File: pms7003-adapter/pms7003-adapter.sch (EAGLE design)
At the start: 4 parts, among them J1 LPPB052CFFN-RC

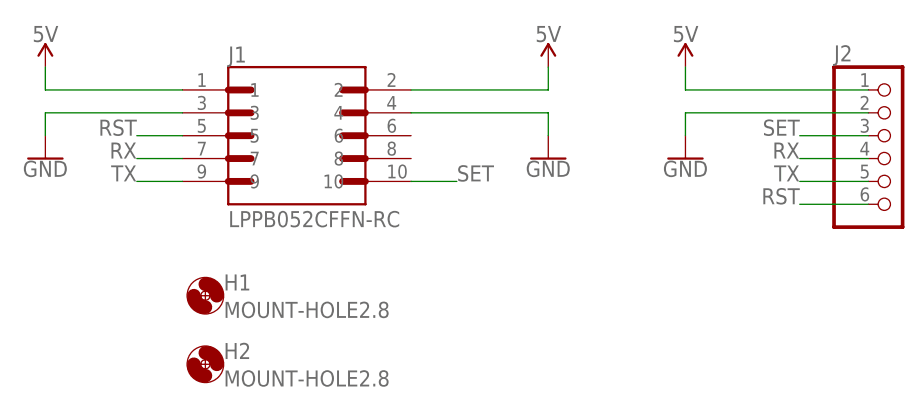
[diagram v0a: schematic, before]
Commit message: Reduced size of the PMS7003 adapter, replaced THT header with SMD header
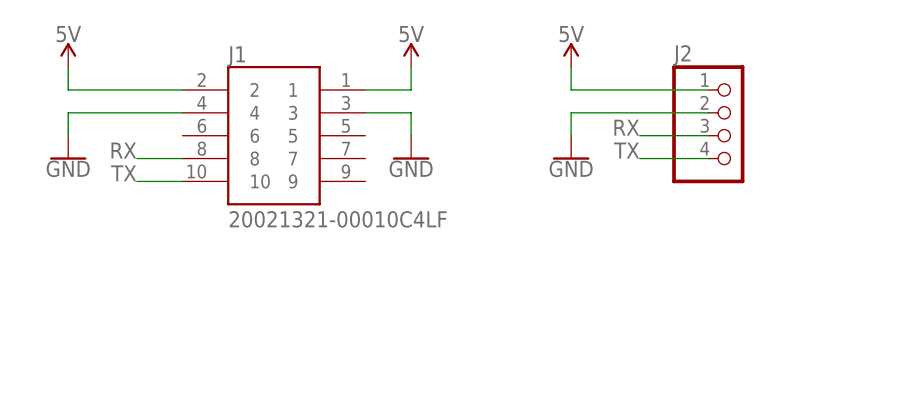
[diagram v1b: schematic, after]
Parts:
- removed H1, H2: MOUNT-HOLE2.8, holes:MOUNT-HOLE2.8
- J1: value LPPB052CFFN-RC -> 20021321-00010C4LF; device aqm-parts:LPPB052CFFN-RC -> aqm-parts:20021321-00010C4LF
- J2: device pinhead:PINHD-1X6 -> pinhead:PINHD-1X4
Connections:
- removed net RST: J1.5, J2.6
- removed net SET: J1.10, J2.3
- net RX: now also J1.8, J2.3; no longer J1.7, J2.4
- net TX: now also J1.10, J2.4; no longer J1.9, J2.5

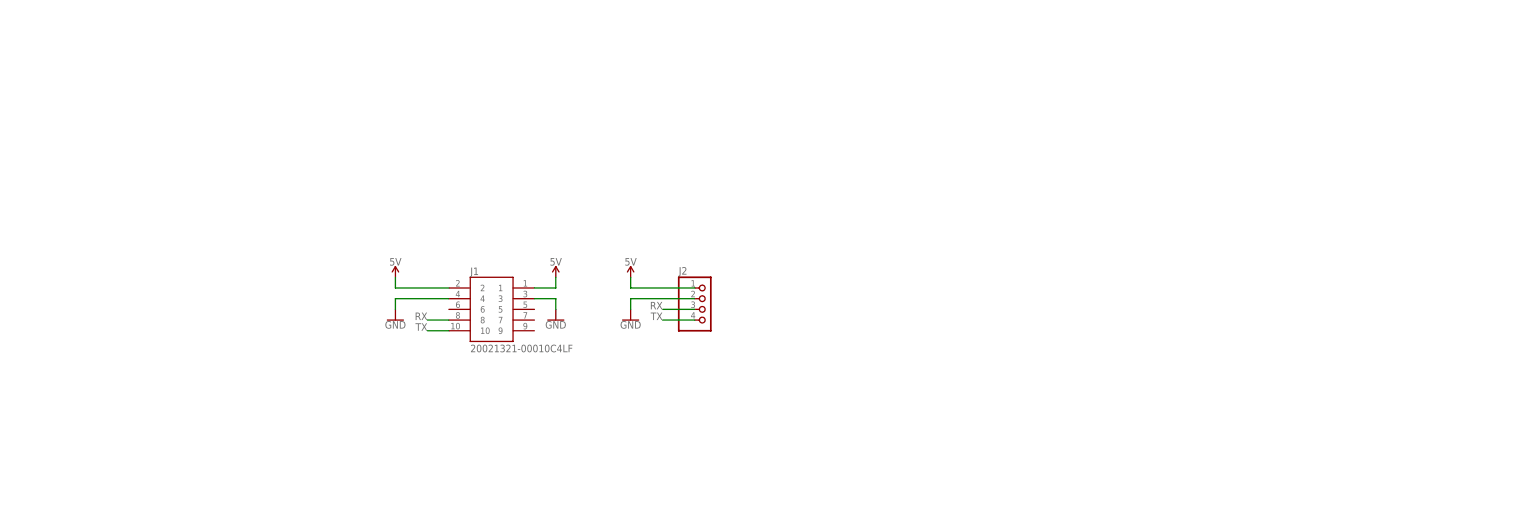
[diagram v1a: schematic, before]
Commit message: Started integrating WiFi into the PMS adapter board
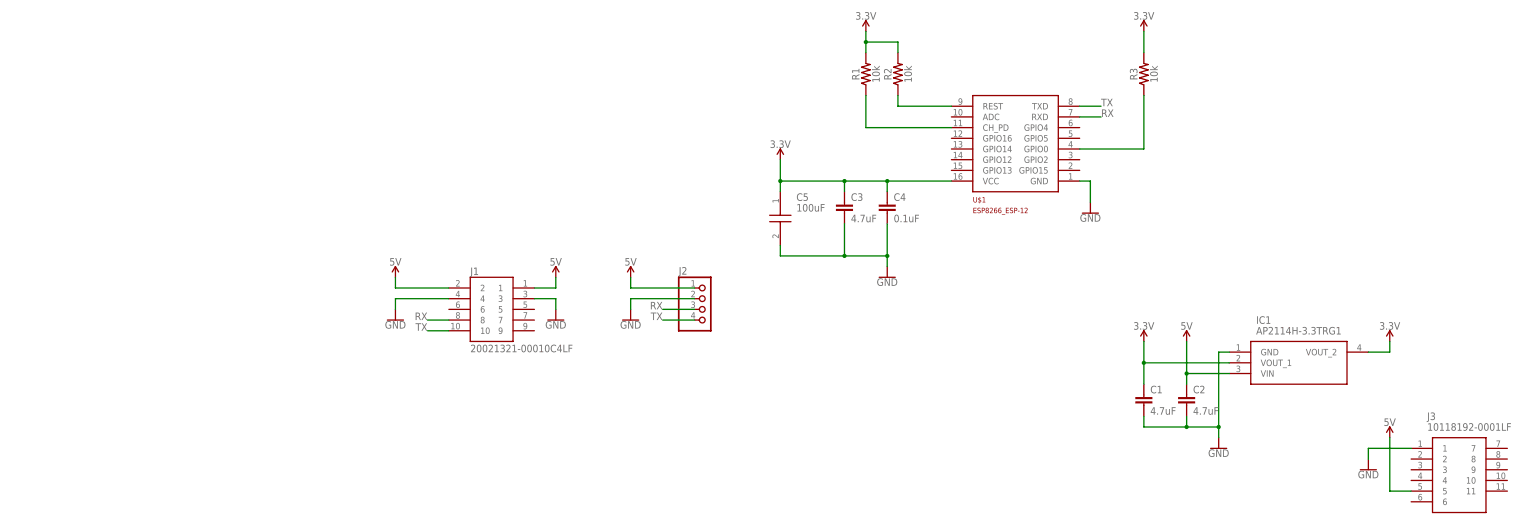
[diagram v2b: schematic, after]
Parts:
- added C1, C2, C3: 4.7uF, SparkFun-Capacitors:4.7UF-0603-6.3V-(10%)
- added C4: 0.1uF, SparkFun-Capacitors:0.1UF-0603-25V-(+80/-20%)
- added C5: 100uF, aqm-parts:JMK316ABJ107ML-T
- added IC1: AP2114H-3.3TRG1, aqm-parts:AP2114H-3.3TRG1
- added J3: 10118192-0001LF, aqm-parts:10118192-0001LF
- added R1, R2, R3: 10k, SparkFun-Resistors:10KOHM-0603-1/10W-1%
- added U$1: ESP8266_ESP-12, aqm-parts:ESP8266_ESP-12
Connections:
- new net 3.3V: C1.1, C3.1, C4.1, C5.1, IC1.VOUT_1, IC1.VOUT_2, R1.2, R2.2, R3.2, U$1.VCC
- new net N$1: R3.1, U$1.GPIO0
- new net N$2: R2.1, U$1.REST
- new net N$3: R1.1, U$1.CH_PD
- net 5V: now also C2.1, IC1.VIN, J3.5
- net GND: now also C1.2, C2.2, C3.2, C4.2, C5.2, IC1.GND, J3.1, U$1.GND
- net RX: now also U$1.RXD
- net TX: now also U$1.TXD

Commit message: Returned to modular design, no cables needed
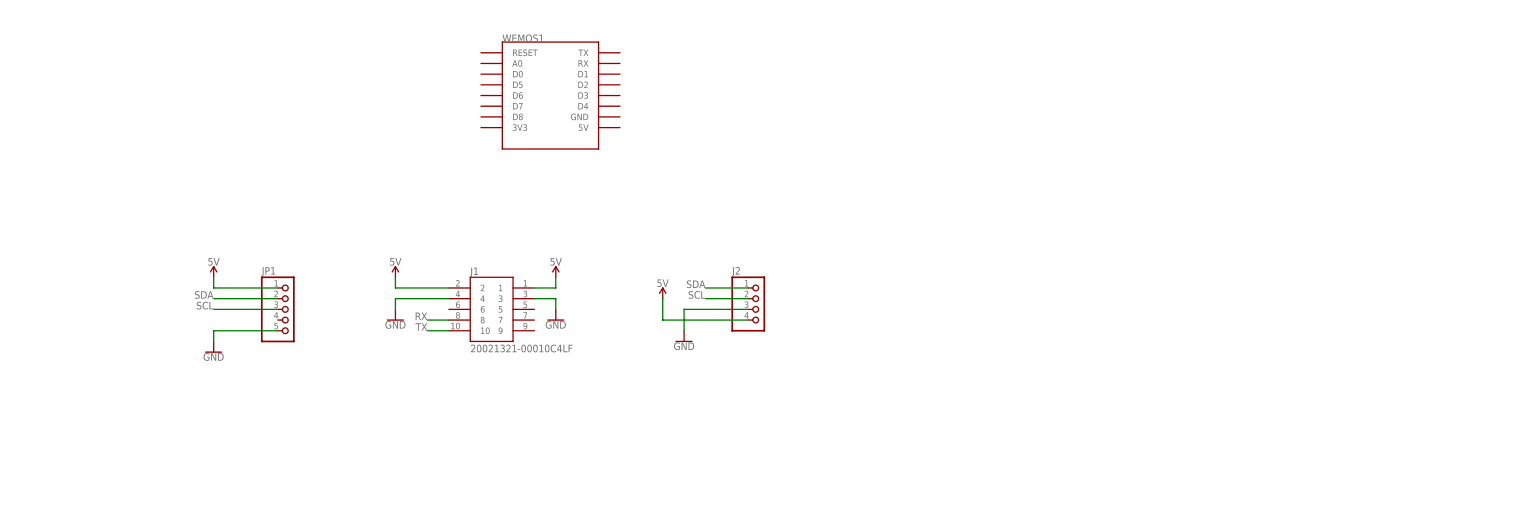
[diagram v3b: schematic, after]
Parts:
- removed C1, C2, C3: 4.7uF, SparkFun-Capacitors:4.7UF-0603-6.3V-(10%)
- removed C4: 0.1uF, SparkFun-Capacitors:0.1UF-0603-25V-(+80/-20%)
- removed C5: 100uF, aqm-parts:JMK316ABJ107ML-T
- removed IC1: AP2114H-3.3TRG1, aqm-parts:AP2114H-3.3TRG1
- removed J3: 10118192-0001LF, aqm-parts:10118192-0001LF
- removed R1, R2, R3: 10k, SparkFun-Resistors:10KOHM-0603-1/10W-1%
- removed U$1: ESP8266_ESP-12, aqm-parts:ESP8266_ESP-12
- added JP1: (no value), pinhead:PINHD-1X5
- added WEMOS1: (no value), aqm-parts:WEMOS-D1-MINI
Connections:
- removed net 3.3V: C1.1, C3.1, C4.1, C5.1, IC1.VOUT_1, IC1.VOUT_2, R1.2, R2.2, R3.2, U$1.VCC
- removed net N$1: R3.1, U$1.GPIO0
- removed net N$2: R2.1, U$1.REST
- removed net N$3: R1.1, U$1.CH_PD
- new net SCL: J2.2, JP1.3
- new net SDA: J2.1, JP1.2
- net 5V: now also J2.4, JP1.1; no longer C2.1, IC1.VIN, J2.1, J3.5
- net GND: now also J2.3, JP1.5; no longer C1.2, C2.2, C3.2, C4.2, C5.2, IC1.GND, J2.2, J3.1, U$1.GND
- net RX: no longer J2.3, U$1.RXD
- net TX: no longer J2.4, U$1.TXD
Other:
- moved on the sheet: J2

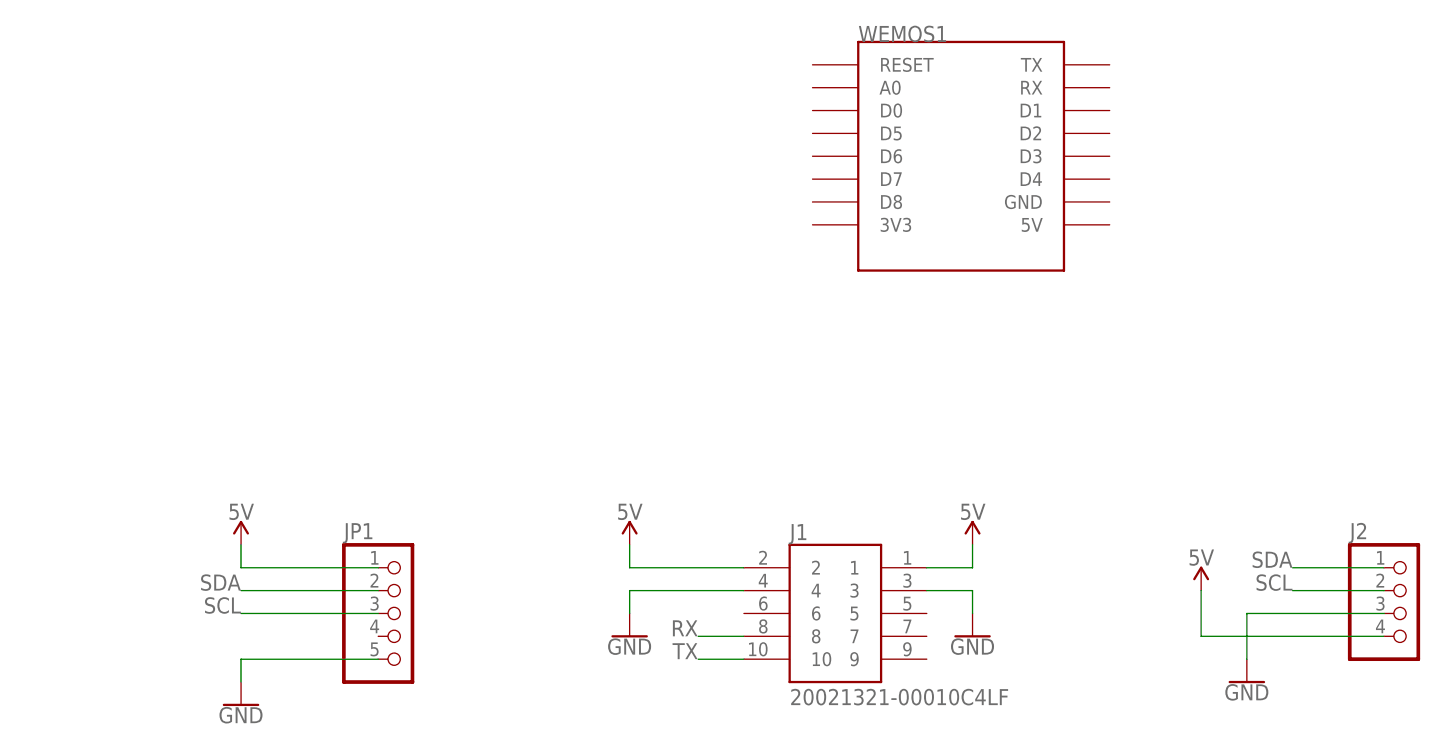
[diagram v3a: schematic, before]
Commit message: Optimized design size with D1 Mini
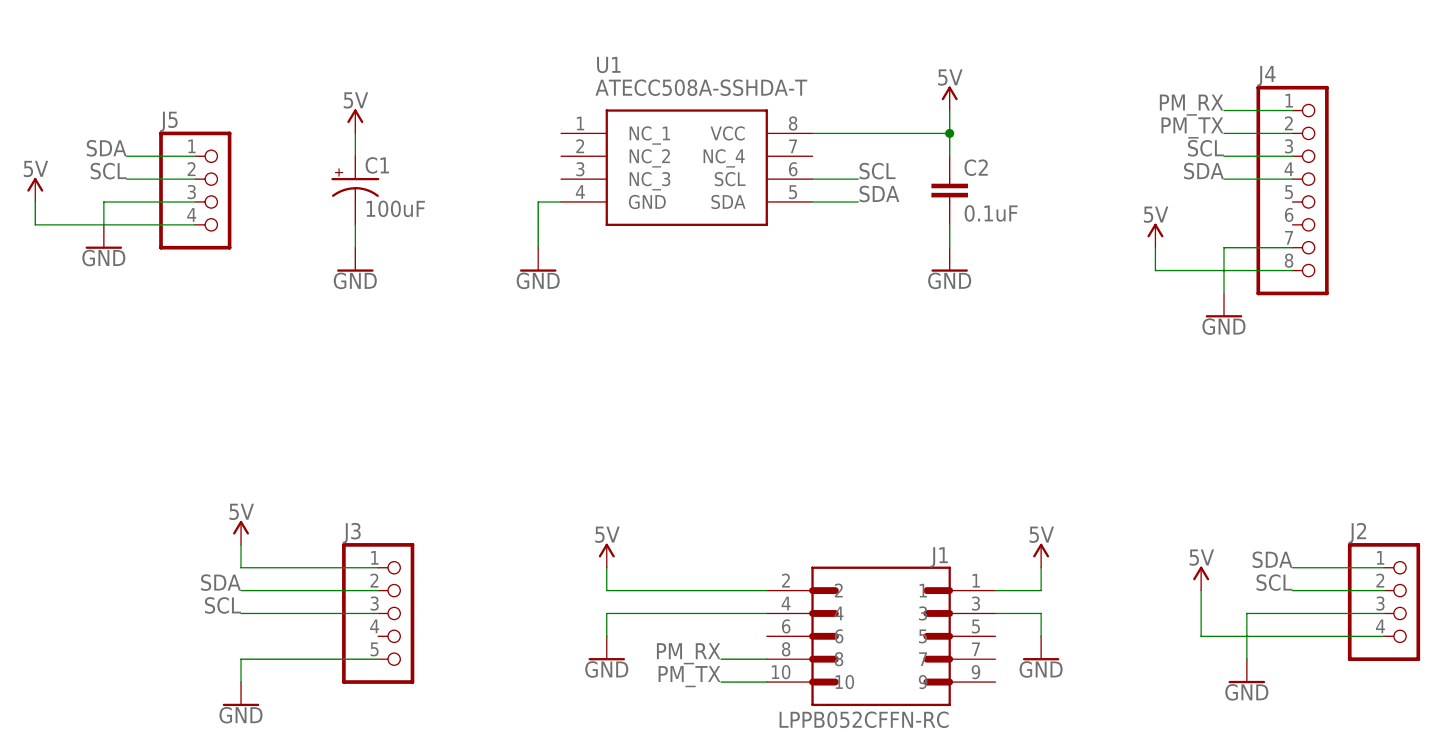
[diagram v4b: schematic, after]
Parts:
- removed WEMOS1: (no value), aqm-parts:WEMOS-D1-MINI
- added C1: 100uF, SparkFun-Capacitors:100UF-POLAR-RADIAL-2.5MM-25V-20%
- added C2: 0.1uF, SparkFun-Capacitors:0.1UF-0603-25V-(+80/-20%)
- added J4: (no value), pinhead:PINHD-1X8
- added J5: (no value), pinhead:PINHD-1X4
- added U1: ATECC508A-SSHDA-T, aqm-parts:ATECC508A-SSHDA-T
- J1: value 20021321-00010C4LF -> LPPB052CFFN-RC; device aqm-parts:20021321-00010C4LF -> aqm-parts:LPPB052CFFN-RC
- renumbered JP1 to J3
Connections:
- removed net RX: J1.8
- removed net TX: J1.10
- new net PM_RX: J1.8, J4.1
- new net PM_TX: J1.10, J4.2
- net 5V: now also C1.+, C2.1, J4.8, J5.4, U1.VCC
- net GND: now also C1.-, C2.2, J4.7, J5.3, U1.GND
- net SCL: now also J4.3, J5.2, U1.SCL
- net SDA: now also J4.4, J5.1, U1.SDA

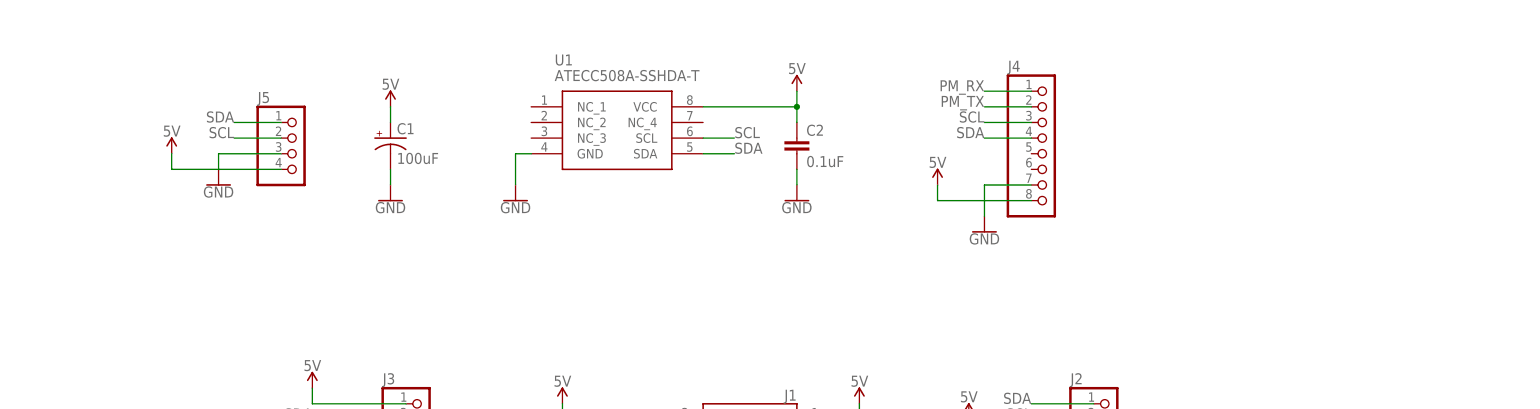
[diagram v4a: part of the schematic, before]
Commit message: Refactored for CO2 sensor and different UART pins
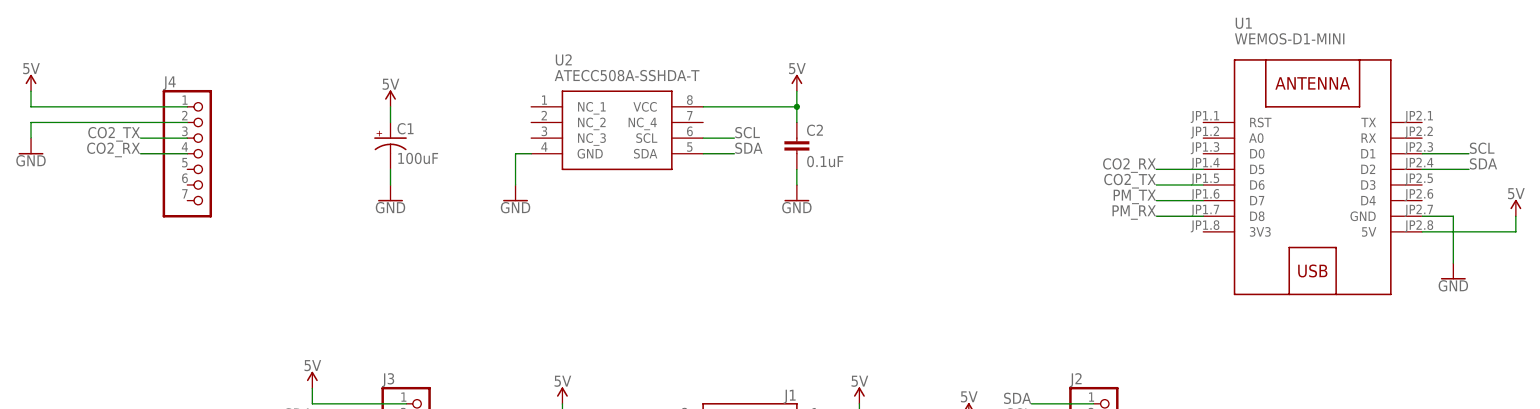
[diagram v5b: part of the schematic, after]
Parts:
- removed J5: (no value), pinhead:PINHD-1X4
- added U2: ATECC508A-SSHDA-T, aqm-parts:ATECC508A-SSHDA-T
- J4: device pinhead:PINHD-1X8 -> pinhead:PINHD-1X7
- U1: value ATECC508A-SSHDA-T -> WEMOS-D1-MINI; device aqm-parts:ATECC508A-SSHDA-T -> aqm-parts:WEMOS-D1-MINI
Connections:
- new net CO2_RX: J4.4, U1.D5
- new net CO2_TX: J4.3, U1.D6
- net 5V: now also J4.1, U1.5V, U2.VCC; no longer J4.8, J5.4, U1.VCC
- net GND: now also J4.2, U2.GND; no longer J4.7, J5.3
- net PM_RX: now also U1.D8; no longer J4.1
- net PM_TX: now also U1.D7; no longer J4.2
- net SCL: now also U1.D1, U2.SCL; no longer J4.3, J5.2, U1.SCL
- net SDA: now also U1.D2, U2.SDA; no longer J4.4, J5.1, U1.SDA
